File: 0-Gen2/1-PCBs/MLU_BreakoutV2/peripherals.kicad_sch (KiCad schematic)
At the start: 58 parts, among them J1 430450422, J17 430450422, J18 430450422, J19 430450422, J2 430450422, J20 430450228, J21 430450228, J22 430450228, J23 430450228, J24 430450422, J25 430450228, J26 430450821, J3 Conn_01x03_Pin

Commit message: [changes] MLUv2
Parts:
- added C2: 0.1uF, ImportedV2:K104K15X7RF5TL2_VIS, symbol Device:C
- added H1, H23, H24: Molex 4 Pin Male, symbol Mechanical:MountingHole
- added H2: Molex 10 Pin Male, symbol Mechanical:MountingHole
- added H22: Molex Socket Crimps, symbol Mechanical:MountingHole
- added H3: Socket for Teensy, symbol Mechanical:MountingHole
- added J10: Conn_02x03_Odd_Even, Connector_PinHeader_2.00mm:PinHeader_2x03_P2.00mm_Vertical, symbol Connector_Generic:Conn_02x03_Odd_Even
- added J12: PixHawk PM02, Connector_PinSocket_2.54mm:PinSocket_1x06_P2.54mm_Vertical, symbol Connector:Conn_01x06_Pin
- added J28, J29: Conn_01x04_Socket, symbol Connector:Conn_01x04_Socket
- added J30, J31: Conn_01x02_Socket, symbol Connector:Conn_01x02_Socket
- added J4: 430450422, ImportedV2:CONN_SD-43045-009_04_MOL, symbol Imported:430450422
- added J5: 430451027, ImportedV2:CONN_SD-43045-010_10_MOL, symbol Imported:430451027
- added J8: Conn_02x22_Odd_Even, Connector_PinSocket_2.54mm:PinSocket_2x22_P2.54mm_Vertical, symbol Connector_Generic:Conn_02x22_Odd_Even
- added J9: J1B1211CCD, ImportedV2:J1B1211CCD, symbol Imported:J1B1211CCD
- added JP40: Jumper_3_Bridged12, Jumper:SolderJumper-3_P1.3mm_Bridged2Bar12_RoundedPad1.0x1.5mm, symbol Jumper:Jumper_3_Bridged12
- added JP41, JP46, JP47, JP48, JP49, JP50, JP51, JP52: Jumper_2_Small_Bridged, Jumper:SolderJumper-2_P1.3mm_Bridged2Bar_RoundedPad1.0x1.5mm, symbol Jumper:Jumper_2_Small_Bridged
- added JP42, JP43, JP44, JP45, JP53, JP54, JP55, JP56, JP57, JP58, JP59, JP60: Jumper_2_Small_Open, Jumper:SolderJumper-2_P1.3mm_Open_RoundedPad1.0x1.5mm, symbol Jumper:Jumper_2_Small_Open
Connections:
- net +3.3V: now also J8.19 (Pin_19), J8.3 (Pin_3)
- net +5V: now also J12.1 (Pin_1), J12.2 (Pin_2), J4.4, J5.1, J8.1 (Pin_1), J8.17 (Pin_17), JP40.1 (A)
- net D/A20: now also J8.9 (Pin_9)
- net D/A21: now also J8.11 (Pin_11)
- net D/A22: now also J8.13 (Pin_13)
- net D/A23: now also J8.15 (Pin_15)
- net GND: now also C2.1, J10.4 (Pin_4), J12.5 (Pin_5), J12.6 (Pin_6), J4.2, J5.2, J8.18 (Pin_18), J8.2 (Pin_2), J8.20 (Pin_20), J8.34 (Pin_34), J8.4 (Pin_4), J8.43 (Pin_43), J9.8 (GND), J9.9, JP46.2 (B), JP51.2 (B); no longer J1.2, J2.2
- net Host_D+: now also J8.23 (Pin_23)
- net Host_D-: now also J8.21 (Pin_21)
- net I2C1_SCL: now also J8.7 (Pin_7), JP47.2 (B), JP50.2 (B); no longer J1.3, J2.3
- net I2C1_SDA: now also J8.5 (Pin_5), JP48.2 (B), JP52.2 (B); no longer J1.1, J2.1
- net UART_RX2: now also J8.26 (Pin_26)
- net UART_RX3: now also J8.30 (Pin_30)
- net UART_TX2: now also J8.28 (Pin_28)
- net UART_TX3: now also J8.32 (Pin_32)
- net at J19.3, JP14.1 (A), JP15.2 (B)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: now also JP60.1 (A)
- net at J24.1, JP18.2 (B), JP19.1 (A)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: now also JP57.1 (A)
- net at J24.3, JP21.1 (A), JP22.2 (B)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: now also JP58.1 (A)
- net at J19.1, JP11.2 (B), JP12.1 (A)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: now also JP59.1 (A)
- net at J2.4: now also JP42.2 (B), JP49.1 (A); no longer JP2.2 (C)
- net at J1.4: now also JP41.1 (A), JP56.2 (B); no longer JP1.2 (C)
- net Dleak renamed xDleak
- new net: J29.1 (Pin_1), JP56.1 (A)
- new net: J28.1 (Pin_1), JP42.1 (A)
- new net: J28.2 (Pin_2), JP43.1 (A)
- new net: J28.3 (Pin_3), JP44.1 (A)
- new net: J28.4 (Pin_4), JP45.1 (A)
- new net: JP2.2 (C), JP49.2 (B)
- new net: J2.3, JP43.2 (B), JP47.1 (A)
- new net: J1.1, JP52.1 (A), JP53.2 (B)
- new net: J1.2, JP51.1 (A), JP54.2 (B)
- new net: J1.3, JP50.1 (A), JP55.2 (B)
- new net: JP1.2 (C), JP41.2 (B)
- new net: J29.3 (Pin_3), JP54.1 (A)
- new net: J31.1 (Pin_1), JP60.2 (B)
- new net: J31.2 (Pin_2), JP59.2 (B)
- new net: J30.1 (Pin_1), JP58.2 (B)
- new net: J30.2 (Pin_2), JP57.2 (B)
- new net: C2.2, J9.2, J9.5
- new net: J2.2, JP44.2 (B), JP46.1 (A)
- new net: J5.8, JP40.2 (C)
- new net: J2.1, JP45.2 (B), JP48.1 (A)
- new net: J29.2 (Pin_2), JP55.1 (A)
- new net: J29.4 (Pin_4), JP53.1 (A)
- new net Analog_Current: J12.3 (Pin_3)
- new net Analog_Voltage: J12.4 (Pin_4)
- new net DISP_DC: J5.5
- new net DISP_LED: J8.12 (Pin_12), JP40.3 (B)
- new net DISP_RST: J5.4
- new net Device_D+: J8.27 (Pin_27)
- new net Device_D-: J8.25 (Pin_25)
- new net D/A14: J8.10 (Pin_10)
- new net I2C2_SCL: J8.8 (Pin_8)
- new net I2C2_SDA: J8.6 (Pin_6)
- new net LED: J10.3 (Pin_3), J9.10
- new net R+: J10.1 (Pin_1), J9.4
- new net R-: J10.2 (Pin_2), J9.6
- new net SPI_CS1: J5.3
- new net SPI_MISO: J5.9
- new net SPI_MOSI: J5.6
- new net SPI_SCK: J5.7
- new net T+: J10.6 (Pin_6), J9.1
- new net T-: J10.5 (Pin_5), J9.3
- new net UART_RX1: J8.24 (Pin_24)
- new net UART_TX1: J8.22 (Pin_22)
- new net outNEO_CTRL_ESCs: J8.31 (Pin_31)
- new net outNEO_CTRL_EXTs: J4.3, J8.35 (Pin_35)
- new net outNEO_CTRL_MLU: J8.39 (Pin_39)
- new net toNEO_CTRL_ESCs: J8.29 (Pin_29)
- new net toNEO_CTRL_EXTs: J4.1, J8.33 (Pin_33)
- new net toNEO_CTRL_MLU: J8.37 (Pin_37)
- new net toNEO_CTRL_Orin: J8.41 (Pin_41)
- new net xD0: J8.14 (Pin_14)
- new net xD1: J8.16 (Pin_16)
- new net xD2: J8.36 (Pin_36)
- new net xD3: J8.38 (Pin_38)
- new net xD4: J8.40 (Pin_40)
- new net xD5: J8.42 (Pin_42)
- new net xD6: J8.44 (Pin_44)
- no-connect marks 0 -> 6
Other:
- note added: "-Route with diff pairs -Avoid vias"
- note added: "2.2" TFT Screen"
- note added: "Ethernet Breakout"
- note added: "Extra Pin Breakout"
- note added: "More info: https://oshpark.com/shared_projects/wUFt1emZ https://www.pjrc.com/store/ethernet_kit.html"
- note added: "Neo_Interface_Exts"
- note added: "Power In"
- note added: "Transition to not using this when Orin board is installed"
- note added: "Vertical Blanks"
- note added: "https://www.amazon.com/dp/B01CZL6QIQ?ref_=ppx_hzsearch_conn_dt_b_fed_asin_title_2"
- note added: "pick whether to chain from ESC board or have on new pin"
- note removed: "Blanks"
- moved on the sheet: J3, JP2

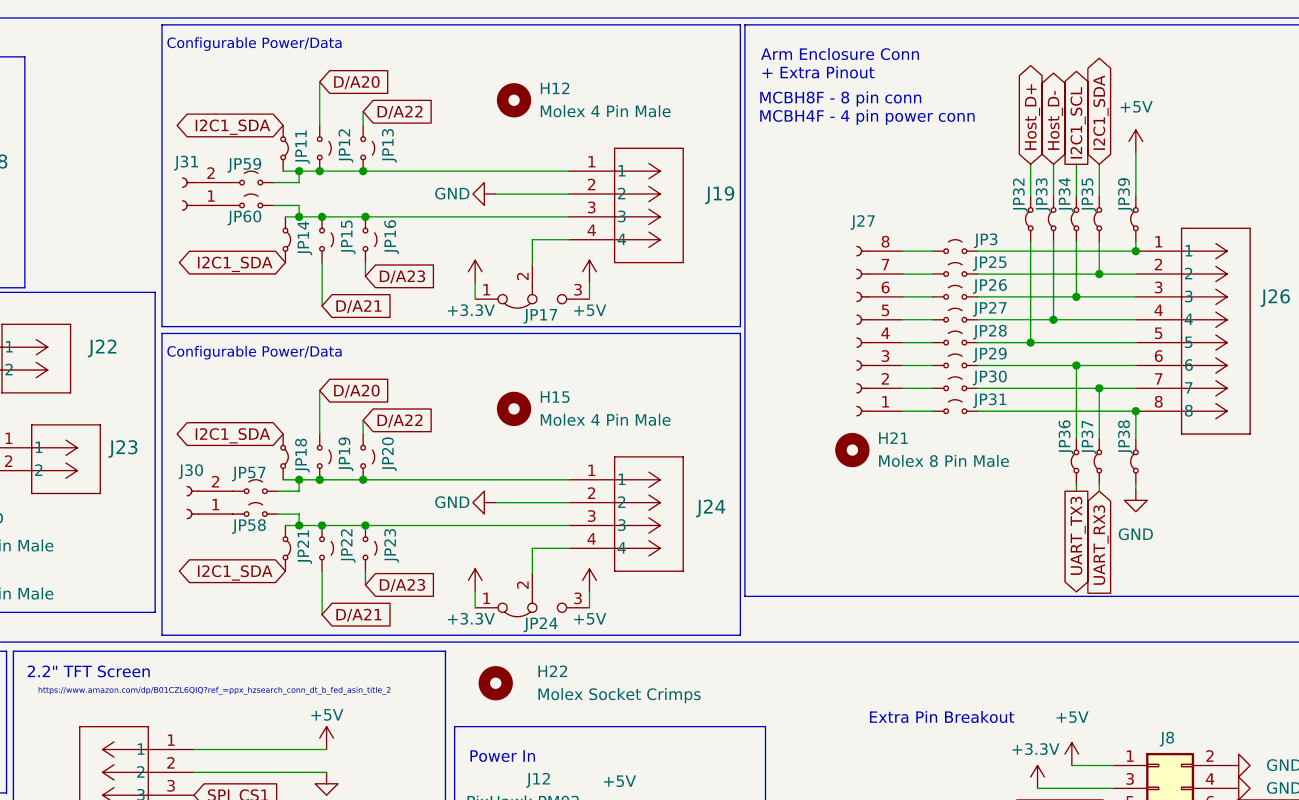
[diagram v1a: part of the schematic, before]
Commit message: [add] major layout updates
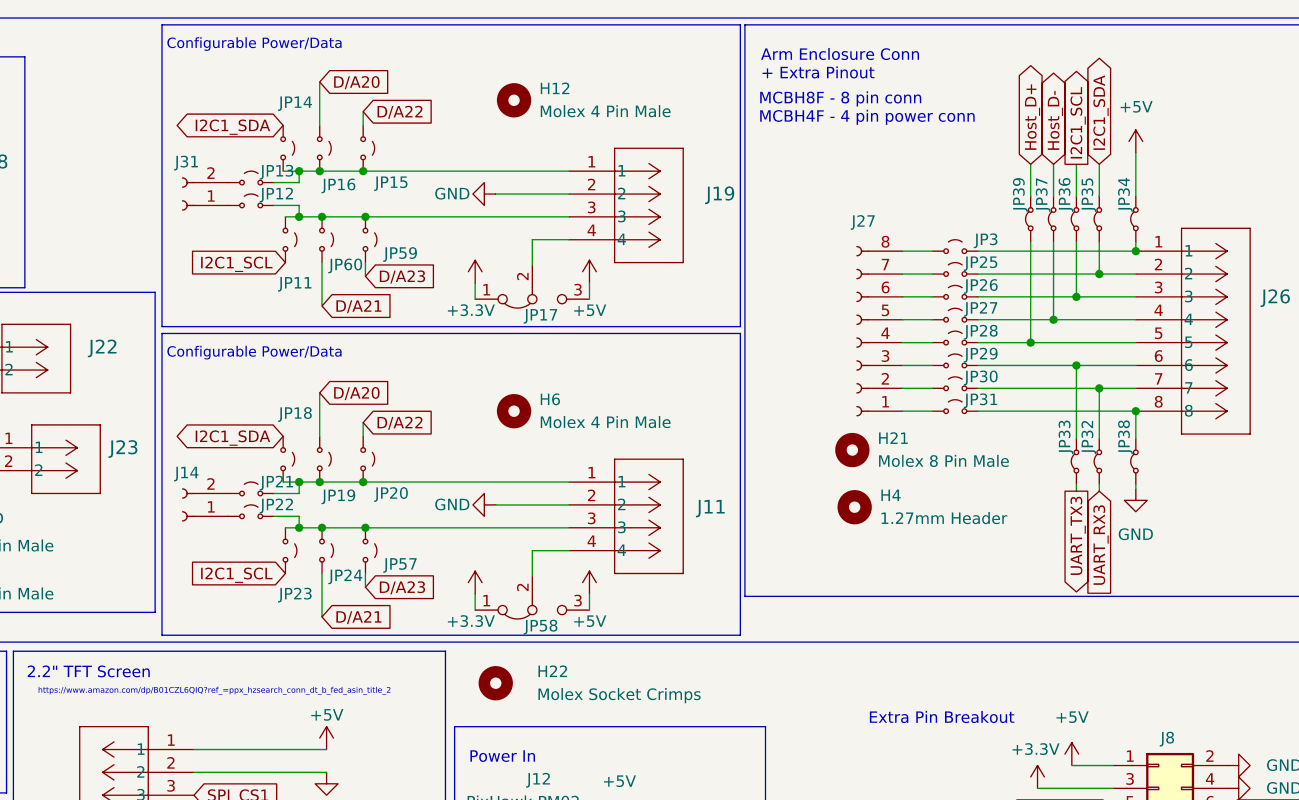
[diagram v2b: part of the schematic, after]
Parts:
- removed H15: Molex 4 Pin Male, symbol Mechanical:MountingHole
- removed J24: 430450422, ImportedV2:CONN_SD-43045-008_04_MOL, symbol Imported:430450422
- removed J30: Conn_01x02_Socket, symbol Connector:Conn_01x02_Socket
- removed JP11, JP14, JP18, JP21: Jumper_2_Small_Bridged, Jumper:SolderJumper-2_P1.3mm_Bridged2Bar_RoundedPad1.0x1.5mm, symbol Jumper:Jumper_2_Small_Bridged
- removed JP24: Jumper_3_Bridged12, Jumper:SolderJumper-3_P1.3mm_Bridged2Bar12_RoundedPad1.0x1.5mm, symbol Jumper:Jumper_3_Bridged12
- removed JP58: Jumper_2_Small_Open, Jumper:SolderJumper-2_P1.3mm_Open_RoundedPad1.0x1.5mm, symbol Jumper:Jumper_2_Small_Open
- added H4: 1.27mm Header, symbol Mechanical:MountingHole
- added H6: Molex 4 Pin Male, symbol Mechanical:MountingHole
- added J11: 430450422, ImportedV2:CONN_SD-43045-008_04_MOL, symbol Imported:430450422
- added J14: Conn_01x02_Socket, Connector_PinSocket_2.54mm:PinSocket_1x02_P2.54mm_Vertical, symbol Connector:Conn_01x02_Socket
- added JP11, JP14, JP18, JP21, JP24: Jumper_2_Small_Open, Connector_PinHeader_1.27mm:PinHeader_1x02_P1.27mm_Vertical, symbol Jumper:Jumper_2_Small_Open
- added JP58: Jumper_3_Bridged12, Connector_PinHeader_1.27mm:PinHeader_1x03_P1.27mm_Vertical, symbol Jumper:Jumper_3_Bridged12
- J31: footprint (none) -> Connector_PinSocket_2.54mm:PinSocket_1x02_P2.54mm_Vertical
- JP12, JP13, JP15, JP16, JP19, JP20, JP22, JP23, JP25, JP26, JP27, JP28, JP29, JP3, JP30, JP31, JP57, JP59, JP60: footprint Jumper:SolderJumper-2_P1.3mm_Open_RoundedPad1.0x1.5mm -> Connector_PinHeader_1.27mm:PinHeader_1x02_P1.27mm_Vertical; Supplier 1 (none) -> https://www.digikey.com/en/products/detail/adam-tech/HMSC-G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; Supplier 1 S/N (none) -> 2057-HMSC-G-ND
- JP17: footprint Jumper:SolderJumper-3_P1.3mm_Bridged2Bar12_RoundedPad1.0x1.5mm -> Connector_PinHeader_1.27mm:PinHeader_1x03_P1.27mm_Vertical
- JP32, JP33, JP34, JP35, JP36, JP37, JP38, JP39: footprint Jumper:SolderJumper-2_P1.3mm_Bridged2Bar_RoundedPad1.0x1.5mm -> Connector_PinHeader_1.27mm:PinHeader_1x02_P1.27mm_Vertical; Supplier 1 (none) -> https://www.digikey.com/en/products/detail/adam-tech/HMSC-G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; Supplier 1 S/N (none) -> 2057-HMSC-G-ND
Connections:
- net +3.3V: now also JP58.1 (A)
- net +5V: now also JP34.2 (B), JP58.3 (B); no longer JP39.2 (B)
- net D/A20: now also JP16.1 (A), JP19.1 (A); no longer JP12.2 (B), JP19.2 (B)
- net D/A21: now also JP60.2 (B), JP24.2 (B); no longer JP15.1 (A), JP22.1 (A)
- net D/A22: now also JP15.1 (A), JP20.1 (A); no longer JP13.2 (B), JP20.2 (B)
- net D/A23: now also JP57.2 (B), JP59.2 (B); no longer JP16.1 (A), JP23.1 (A)
- net GND: now also J11.2
- net Host_D+: now also JP39.2 (B); no longer JP32.2 (B)
- net Host_D-: now also JP37.2 (B); no longer JP33.2 (B)
- net I2C1_SCL: now also JP23.2 (B), JP36.2 (B), JP11.2 (B); no longer JP34.2 (B)
- net I2C1_SDA: now also JP14.1 (A), JP18.1 (A)
- net UART_RX3: now also JP32.1 (A); no longer JP37.1 (A)
- net UART_TX3: now also JP33.1 (A); no longer JP36.1 (A)
- net at J19.3, JP60.1 (A): now also JP12.2 (B), JP59.1 (A), JP11.1 (A); no longer JP15.2 (B), JP16.2 (B)
- net at JP22.2 (B): now also JP23.1 (A), JP57.1 (A), J11.3, JP24.1 (A); no longer JP23.2 (B)
- net at J26.1, JP3.2 (B): now also JP34.1 (A); no longer JP39.1 (A)
- net at J31.1 (Pin_1): now also JP12.1 (A); no longer JP60.2 (B)
- net at J31.2 (Pin_2): now also JP13.1 (A); no longer JP59.2 (B)
- net at J26.3, JP26.2 (B): now also JP36.1 (A); no longer JP34.1 (A)
- net at J26.4, JP27.2 (B): now also JP37.1 (A); no longer JP33.1 (A)
- net at J26.5, JP28.2 (B): now also JP39.1 (A); no longer JP32.1 (A)
- net at J26.6, JP29.2 (B): now also JP33.2 (B); no longer JP36.2 (B)
- net at J26.7, JP30.2 (B): now also JP32.2 (B); no longer JP37.2 (B)
- new net: J11.1, JP18.2 (B), JP19.2 (B), JP20.2 (B), JP21.2 (B)
- new net: J11.4, JP58.2 (C)
- new net: J19.1, JP13.2 (B), JP14.2 (B), JP15.2 (B), JP16.2 (B)
- new net: J14.1 (Pin_1), JP22.1 (A)
- new net: J14.2 (Pin_2), JP21.1 (A)

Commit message: [final pass] MLU breakout
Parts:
- removed J1: 430450422, ImportedV2:CONN_SD-43045-009_04_MOL, symbol Imported:430450422
- removed J29: Conn_01x04_Socket, symbol Connector:Conn_01x04_Socket
- removed JP1: Jumper_3_Bridged12, Jumper:SolderJumper-3_P1.3mm_Bridged2Bar12_RoundedPad1.0x1.5mm, symbol Jumper:Jumper_3_Bridged12
- removed JP41, JP49, JP50, JP51, JP52: Jumper_2_Small_Bridged, Jumper:SolderJumper-2_P1.3mm_Bridged2Bar_RoundedPad1.0x1.5mm, symbol Jumper:Jumper_2_Small_Bridged
- removed JP45, JP53, JP54, JP55, JP56: Jumper_2_Small_Open, Jumper:SolderJumper-2_P1.3mm_Open_RoundedPad1.0x1.5mm, symbol Jumper:Jumper_2_Small_Open
- added H8, H9: ~, MountingHole:MountingHole_3.2mm_M3, symbol Mechanical:MountingHole
- added JP45: Jumper_2_Small_Bridged, Connector_PinHeader_1.27mm:PinHeader_1x02_P1.27mm_Vertical, symbol Jumper:Jumper_2_Small_Bridged
- added JP67: Jumper_2_Small_Open, Connector_PinHeader_1.27mm:PinHeader_1x02_P1.27mm_Vertical, symbol Jumper:Jumper_2_Small_Open
- J28: footprint (none) -> Connector_PinSocket_2.54mm:PinSocket_1x04_P2.54mm_Vertical
- JP2, JP40: footprint Jumper:SolderJumper-3_P1.3mm_Bridged2Bar12_RoundedPad1.0x1.5mm -> Connector_PinHeader_1.27mm:PinHeader_1x03_P1.27mm_Vertical
- JP42, JP43, JP44: footprint Jumper:SolderJumper-2_P1.3mm_Open_RoundedPad1.0x1.5mm -> Connector_PinHeader_1.27mm:PinHeader_1x02_P1.27mm_Vertical; Supplier 1 (none) -> https://www.digikey.com/en/products/detail/adam-tech/HMSC-G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; Supplier 1 S/N (none) -> 2057-HMSC-G-ND
- JP46, JP47, JP48: footprint Jumper:SolderJumper-2_P1.3mm_Bridged2Bar_RoundedPad1.0x1.5mm -> Connector_PinHeader_1.27mm:PinHeader_1x02_P1.27mm_Vertical; Supplier 1 (none) -> https://www.digikey.com/en/products/detail/adam-tech/HMSC-G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; Supplier 1 S/N (none) -> 2057-HMSC-G-ND
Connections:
- net GND: no longer C2.1, J10.4 (Pin_4), J9.8 (GND), J9.9
- net I2C1_SDA: now also JP45.2 (B); no longer JP48.2 (B)
- net at JP42.1 (A): now also J28.3 (Pin_3); no longer J28.1 (Pin_1)
- net at JP44.1 (A): now also J28.1 (Pin_1); no longer J28.3 (Pin_3)
- net at J28.4 (Pin_4): now also JP67.1 (A)
- net at JP42.2 (B): now also J2.2, JP46.1 (A); no longer J2.4
- net at JP2.2 (C): now also JP48.2 (B)
- net at JP48.1 (A): now also J2.4, JP44.2 (B); no longer J2.1
- new net: J2.1, JP45.1 (A), JP67.2 (B)
- new net ETH_GND: C2.1, J10.4 (Pin_4), J9.8 (GND), J9.9
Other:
- moved on the sheet: J3

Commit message: [add] beginning routing
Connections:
- net UART_RX1: now also J8.22 (Pin_22); no longer J8.24 (Pin_24)
- net UART_TX1: now also J8.24 (Pin_24); no longer J8.22 (Pin_22)
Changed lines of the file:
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@@
 	(global_label "UART_RX1"
 		(shape input)
-		(at 239.776 128.778 0)
-		(fields_autoplaced yes)
-		(effects
-			(font
-				(size 1.27 1.27)
-			)
-			(justify left)
-		)
-		(property "Intersheetrefs" "${INTERSHEET_REFS}"
-			(at 252.0745 128.778 0)
+		(at 239.776 126.238 0)
+		(fields_autoplaced yes)
+		(effects
+			(font
+				(size 1.27 1.27)
+			)
+			(justify left)
+		)
+		(property "Intersheetrefs" "${INTERSHEET_REFS}"
+			(at 252.0745 126.238 0)
 			(effects
 				(font
@@
 	(global_label "UART_TX1"
 		(shape output)
-		(at 239.776 126.238 0)
-		(fields_autoplaced yes)
-		(effects
-			(font
-				(size 1.27 1.27)
-			)
-			(justify left)
-		)
-		(property "Intersheetrefs" "${INTERSHEET_REFS}"
-			(at 251.7721 126.238 0)
-			(effects
-				(font
+		(at 239.776 128.778 0)
+		(fields_autoplaced yes)
+		(effects
+			(font
+				(size 1.27 1.27)
+			)
+			(justify left)
+		)
+		(property "Intersheetrefs" "${INTERSHEET_REFS}"
+			(at 251.7721 128.778 0)
+			(effects
+				(font

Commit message: before restructure
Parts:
- renumbered C2 to C4, H4 to H10, H18 to H11, H19 to H12, H20 to H13, H22 to H14, H8 to H15, H9 to H16, H2 to H17, H23 to H18, H24 to H19, H1 to H20, H3 to H21, H12 to H3, H13 to H4, H14 to H5, H16 to H7, H17 to H8, H21 to H9, J21 to J10, J22 to J11, J23 to J12, J11 to J13, J25 to J14, J14 to J15, J5 to J16, J2 to J17, J12 to J18, J28 to J19, J8 to J20, J4 to J21, J3 to J22, J9 to J23, J10 to J24, J17 to J3, J18 to J4, J19 to J5, J31 to J6, J26 to J7, J20 to J8, J27 to J9, JP16 to JP15, JP15 to JP16, JP13 to JP17, JP12 to JP18, JP39 to JP19, JP37 to JP20, JP36 to JP21, JP35 to JP22, JP34 to JP23, JP11 to JP24, JP60 to JP25, JP59 to JP26, JP3 to JP27, JP25 to JP28, JP26 to JP29, JP17 to JP30, JP27 to JP31, JP28 to JP32, JP29 to JP33, JP30 to JP34, JP31 to JP35, JP18 to JP36, JP19 to JP37, JP20 to JP38, JP33 to JP39, JP32 to JP40, JP38 to JP41, JP21 to JP42, JP22 to JP43, JP23 to JP44, JP24 to JP45, JP57 to JP46, JP58 to JP47, JP2 to JP48, JP48 to JP49, JP47 to JP50, JP46 to JP51, JP45 to JP52, JP67 to JP53, JP42 to JP54, JP43 to JP55, JP44 to JP56, JP40 to JP57, R8 to R3, R9 to R4
